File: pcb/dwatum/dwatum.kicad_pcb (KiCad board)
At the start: 2 copper layers, 0 parts

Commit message: starting on layout
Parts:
- added A1: ANT, polypoint:FRACTUS-2.4GHZ-FR05-S1-N-0-102, F.Cu at (193.1, 106.5)
- added B1: 2450BM15A0002, polypoint:2450BM, F.Cu at (172.4, 106.0)
- added C1: 1uF, Capacitors_SMD:C_0402, F.Cu at (196.8, 135.9)
- added C10: 22pF, Capacitors_SMD:C_0402, F.Cu at (195.9, 118.8)
- added C11: 22pF, Capacitors_SMD:C_0402, F.Cu at (189.2, 124.1)
- added C12: 12pF, Capacitors_SMD:C_0402, F.Cu at (200.6, 111.4)
- added C13: 12pF, Capacitors_SMD:C_0402, F.Cu at (183.6, 128.0)
- added C14: 1uF, Capacitors_SMD:C_0402, F.Cu at (204.6, 105.7)
- added C15: 1uF, Capacitors_SMD:C_0402, F.Cu at (192.0, 118.4)
- added C16: 1uF, Capacitors_SMD:C_0402, F.Cu at (196.8, 113.3)
- added C17: 1uF, Capacitors_SMD:C_0402, F.Cu at (179.8, 129.2)
- added C18: 10uF, Capacitors_SMD:C_0603, F.Cu at (185.7, 116.6)
- added C19: 10uF, Capacitors_SMD:C_0603, F.Cu at (176.0, 124.9)
- added C2: 0.1uF, Capacitors_SMD:C_0402, F.Cu at (205.6, 116.9)
- added C20: 1nF, Capacitors_SMD:C_0402, F.Cu at (208.0, 105.7)
- added C3: 0.1uF, Capacitors_SMD:C_0402, F.Cu at (198.4, 124.3)
- added C4: 0.1uF, Capacitors_SMD:C_0402, F.Cu at (193.7, 124.3)
- added C5: 0.1uF, Capacitors_SMD:C_0402, F.Cu at (189.0, 129.6)
- added C6: 0.1uF, Capacitors_SMD:C_0402, F.Cu at (200.9, 116.9)
- added C7: 220pF, Capacitors_SMD:C_0402, F.Cu at (184.1, 133.5)
- added C8: 0.1uF, Capacitors_SMD:C_0402, F.Cu at (205.1, 111.4)
- added C9: 0.1uF, Capacitors_SMD:C_0402, F.Cu at (196.8, 133.3)
- added D1: Led_RGB_CA, polypoint:1mm_SQ_4PAD, F.Cu at (169.1, 124.6)
- added J1: TC2030-CC2538-BL, polypoint:TC2030, F.Cu at (158.0, 106.5)
- added L1: 2.2uH, polypoint:MIPSZ201D, F.Cu at (203.2, 122.2)
- added P1: CONN_01X02, Pin_Headers:Pin_Header_Straight_1x02, F.Cu at (184.2, 109.1)
- added R1: 10K, Resistors_SMD:R_0402, F.Cu at (185.3, 122.4)
- added R2: 10K, Resistors_SMD:R_0402, F.Cu at (179.8, 123.6)
- added R3: 2.2K, Resistors_SMD:R_0402, F.Cu at (174.4, 130.7)
- added R4: 56K, Resistors_SMD:R_0402, F.Cu at (201.1, 105.8)
- added R5: 1K, Resistors_SMD:R_0402, F.Cu at (198.2, 105.8)
- added R6: 1K, Resistors_SMD:R_0402, F.Cu at (171.2, 130.2)
- added R7: 1K, Resistors_SMD:R_0402, F.Cu at (189.1, 118.5)
- added U1: DWM1000, polypoint:DWM1000_REVERSE, F.Cu at (157.1, 123.4)
- added U2: CC2538, polypoint:QFN-56-1EP_8x8mm_Pitch0.5mm, F.Cu at (157.5, 116.8)
- added U3: TPS727xx, polypoint:WSON-8_1.5x1.5mm, F.Cu at (166.1, 130.4)
- added U4: TPS62740, polypoint:R-PWSON-12, F.Cu at (179.6, 117.2)
- added X1: CRYSTAL_SMD_4, polypoint:FA-128, F.Cu at (156.0, 130.0)
- added Y1: Crystal, polypoint:ABS05, F.Cu at (192.2, 113.1)

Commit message: working on pcb placement
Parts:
- U1: footprint polypoint:DWM1000_REVERSE -> polypoint:DWM1000_REVERSE_SMD
- moved C1 65.4 mm to (171.8, 75.5), turned to 90 degrees
- moved C9 61.5 mm to (178.2, 74.8), turned to 270 degrees
- moved L1 58.1 mm to (162.8, 80.5), turned to 270 degrees
- moved C7 56.9 mm to (180.5, 76.8), turned to 270 degrees
- moved X1 54.8 mm to (184.2, 83.0), turned to 90 degrees
- moved C17 54.5 mm to (170.5, 75.5), turned to 90 degrees
- moved C5 53.4 mm to (181.5, 76.8), turned to 270 degrees
- moved C11 50.7 mm to (174.0, 75.8), turned to 180 degrees
- moved C10 49.4 mm to (174.0, 74.5)
- moved C6 47.6 mm to (167.8, 82.8), turned to 180 degrees
- moved C18 47.0 mm to (163.5, 75.2)
- moved C3 46.4 mm to (181.0, 81.2), turned to 180 degrees
- moved U3 46.2 mm to (164.0, 84.2), turned to 90 degrees
- moved C19 45.9 mm to (164.5, 80.5), turned to 90 degrees
- moved C15 45.3 mm to (162.2, 84.2), turned to 270 degrees
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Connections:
- C1 pad 1: +3V3 -> VCC
- C2 pad 1: +3V3 -> VCC
- C3 pad 2: +3V3 -> VCC
- C4 pad 1: +3V3 -> VCC
- C5 pad 2: +3V3 -> VCC
- C6 pad 1: +3V3 -> VCC
- C7 pad 2: +3V3 -> VCC
- C8 pad 1: +3V3 -> VCC
- C9 pad 2: +3V3 -> VCC
- U2 pad 10: +3V3 -> VCC
- U2 pad 15: +3V3 -> VCC
- U2 pad 24: +3V3 -> VCC
- U2 pad 30: LED_BLUE -> LED_GREEN
- U2 pad 31: LED_GREEN -> LED_BLUE
- U2 pad 33: +3V3 -> VCC
- U2 pad 36: +3V3 -> VCC
- U2 pad 40: +3V3 -> VCC
- U2 pad 43: +3V3 -> VCC
- U2 pad 55: +3V3 -> VCC
- X1 pad 2: Net-(C13-Pad1) -> GND
- X1 pad 3: GND -> Net-(C13-Pad1)
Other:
- board outline added: 37.5 x 17.5 mm
- copper layers 2 -> 4

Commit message: most of the routing is done with dwatum
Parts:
- moved P1 29.8 mm to (188.5, 86.0), turned to 0 degrees
- moved J1 6.59 mm to (164.9, 87.7), turned to 0 degrees
- moved A1 4.59 mm to (189.2, 76.2), turned to 90 degrees
- moved C2 0.75 mm to (175.2, 88.2)
- moved C20 0.75 mm to (176.8, 88.2)
- moved R3 0.75 mm to (178.2, 88.2)
- moved C4 0.68 mm to (170.1, 87.7), turned to 180 degrees
- moved C13 0.65 mm to (185.8, 83.0)
- moved D1 0.56 mm to (184.2, 86.8)
- moved U1 0.50 mm to (174.0, 85.5)
- moved X1 0.45 mm to (183.8, 83.0)
- moved C14 0.32 mm to (163.8, 86.0), turned to 0 degrees
- moved C1 0.25 mm to (171.8, 75.2)
- moved C17 0.25 mm to (170.5, 75.2)
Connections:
- U1 pad 5: VCC -> VAA
- U1 pad 6: VCC -> VAA
- U1 pad 7: VCC -> VAA
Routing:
- net +BATT: track 0.00 -> 56.3 mm
- net VAA: track 0.00 -> 47.3 mm, vias 0 -> 1
- net GND: track 0.00 -> 40.1 mm, vias 0 -> 39
- net DW_WAKEUP: track 0.00 -> 34.6 mm, vias 0 -> 3
- net VCC: track 0.00 -> 33.5 mm, vias 0 -> 10
- net ~RESET: track 0.00 -> 15.1 mm, vias 0 -> 3
- net BOOTLOADER_RX: track 0.00 -> 12.6 mm
- net BOOTLOADER_TX: track 0.00 -> 11.4 mm, vias 0 -> 2
- net BOOTLOADER_CTRL: track 0.00 -> 10.6 mm
- net DW_RSTn: track 0.00 -> 8.96 mm, vias 0 -> 1
- net Net-(C13-Pad1): track 0.00 -> 8.28 mm
- net SPI_SCK: track 0.00 -> 8.23 mm, vias 0 -> 1
- net Net-(C12-Pad2): track 0.00 -> 7.96 mm
- net Net-(B1-Pad4): track 0.00 -> 6.89 mm
- net Net-(B1-Pad3): track 0.00 -> 6.85 mm
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- added copper zone on In1.Cu, net GND
- added copper zone on In2.Cu, net VCC
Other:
- board size 37.5 x 17.5 mm -> 31 x 18.5 mm
- rule trace_min: 0.2 -> 0.1524
- rule via_min_drill: 0.3 -> 0.2032
- rule via_min_size: 0.4 -> 0.508
- board text added: "Ben Kempke"
- board text added: "DW1000"
- board text added: "DWAtum v0.1"
- board text added: "Univ. of Mich."

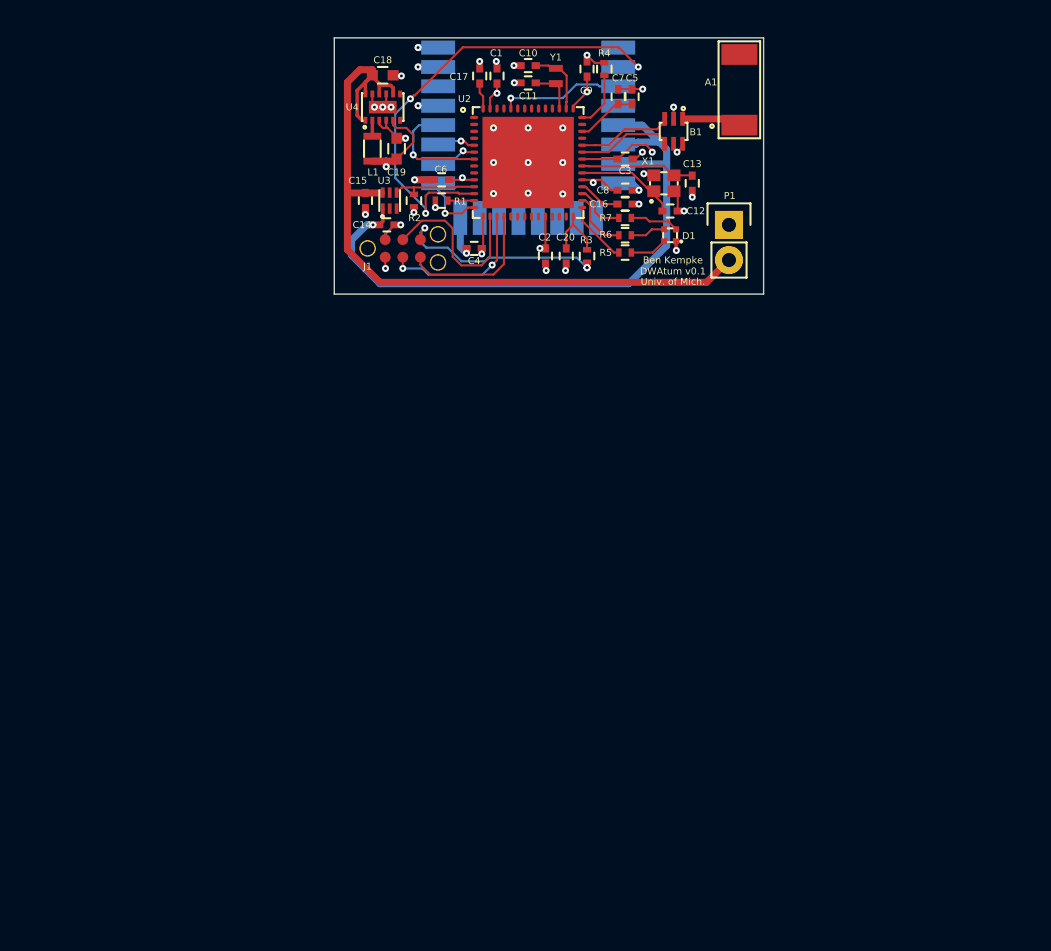
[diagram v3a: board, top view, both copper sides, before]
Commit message: adding atum footprint and starting from scratch with dwatum adapter board
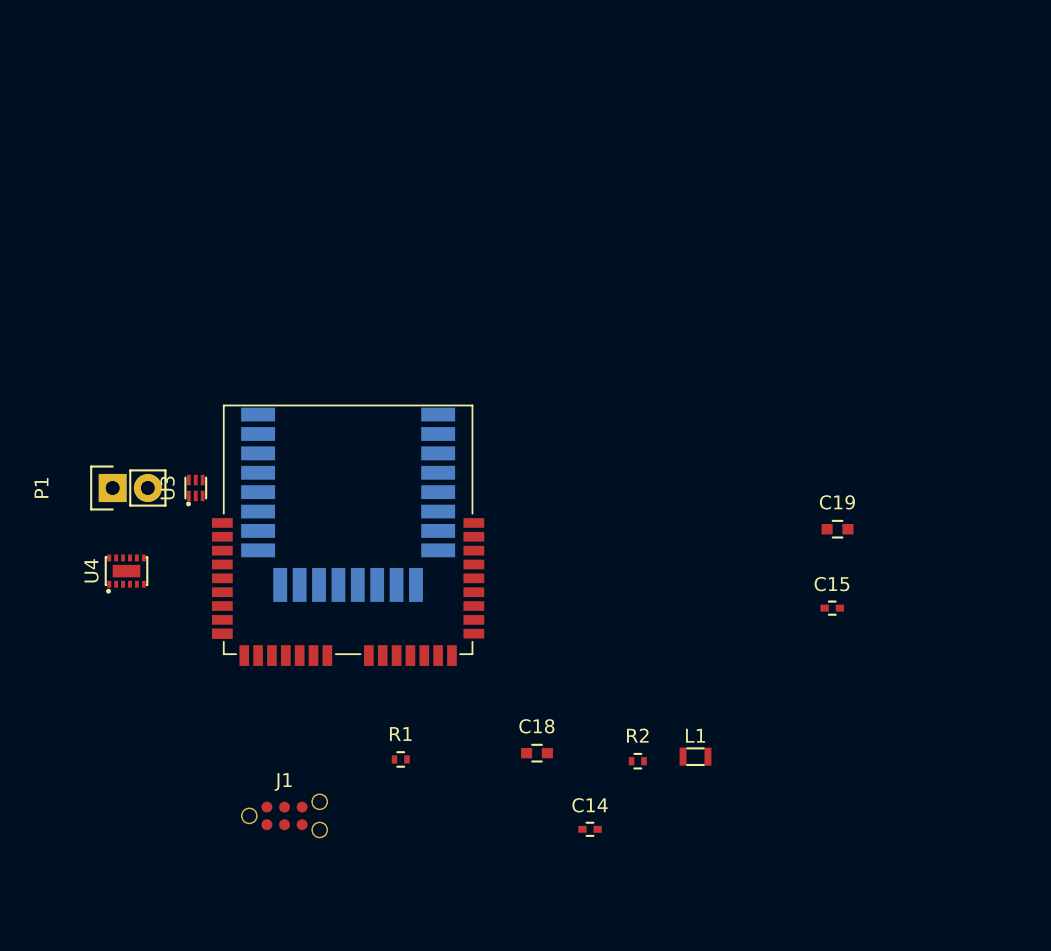
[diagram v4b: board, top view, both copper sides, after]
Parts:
- removed A1: ANT, polypoint:FRACTUS-2.4GHZ-FR05-S1-N-0-102
- removed B1: 2450BM15A0002, polypoint:2450BM
- removed C1, C16, C17: 1uF, Capacitors_SMD:C_0402
- removed C10, C11: 22pF, Capacitors_SMD:C_0402
- removed C12, C13: 12pF, Capacitors_SMD:C_0402
- removed C2, C3, C4, C5, C6, C8, C9: 0.1uF, Capacitors_SMD:C_0402
- removed C20: 1nF, Capacitors_SMD:C_0402
- removed C7: 220pF, Capacitors_SMD:C_0402
- removed D1: Led_RGB_CA, polypoint:1mm_SQ_4PAD
- removed R3: 2.2K, Resistors_SMD:R_0402
- removed R4: 56K, Resistors_SMD:R_0402
- removed R5, R6, R7: 1K, Resistors_SMD:R_0402
- removed X1: CRYSTAL_SMD_4, polypoint:FA-128
- removed Y1: Crystal, polypoint:ABS05
- U2: value CC2538 -> ATUM; footprint polypoint:QFN-56-1EP_8x8mm_Pitch0.5mm -> polypoint:ATUM_SMD
- moved C18 50.2 mm to (174.6, 124.1)
- moved L1 49.7 mm to (186.1, 124.4), turned to 0 degrees
- moved P1 48.4 mm to (144.0, 105.0), turned to 90 degrees
- moved C14 46.0 mm to (178.5, 129.6)
- moved C15 44.7 mm to (196.0, 113.7), turned to 0 degrees
- moved R2 43.6 mm to (181.9, 124.7), turned to 0 degrees
- moved C19 42.1 mm to (196.3, 108.0), turned to 0 degrees
- moved J1 41.9 mm to (156.4, 128.7)
- moved R1 40.5 mm to (164.8, 124.6), turned to 0 degrees
- moved U4 38.3 mm to (145.0, 111.0)
- moved U2 37.8 mm to (161.0, 117.0), turned to 270 degrees
- moved U1 29.5 mm to (161.0, 112.0)
- moved U3 25.0 mm to (150.0, 105.0)
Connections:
- U2 pad 1: Net-(U2-Pad1) -> VCC
- U2 pad 10: VCC -> Net-(U2-Pad10)
- U2 pad 11: DW_PWR_EN -> Net-(U2-Pad11)
- U2 pad 12: DW_WAKEUP -> Net-(U2-Pad12)
- U2 pad 13: DW_IRQ -> Net-(U2-Pad13)
- U2 pad 14: DW_CE -> SPI_MISO
- U2 pad 15: VCC -> SPI_MOSI
- U2 pad 16: BOOTLOADER_RX -> SPI_SCK
- U2 pad 17: BOOTLOADER_TX -> Net-(U2-Pad17)
- U2 pad 18: BOOTLOADER_CTRL -> Net-(U2-Pad18)
- U2 pad 19: Net-(U2-Pad19) -> DW_WAKEUP
- U2 pad 20: Net-(U2-Pad20) -> DW_IRQ
- U2 pad 21: Net-(U2-Pad21) -> DW_CE
- U2 pad 22: Net-(U2-Pad22) -> BOOTLOADER_RX
- U2 pad 23: Net-(U2-Pad23) -> BOOTLOADER_TX
- U2 pad 24: VCC -> BOOTLOADER_CTRL
- U2 pad 29: LED_RED -> Net-(U2-Pad29)
- U2 pad 30: LED_GREEN -> ~RESET
- U2 pad 31: LED_BLUE -> Net-(U2-Pad31)
- U2 pad 32: Net-(C16-Pad1) -> GND
- U2 pad 5: SPI_MISO -> Net-(U2-Pad5)
- U2 pad 6: SPI_MOSI -> Net-(U2-Pad6)
- U2 pad 7: SPI_SCK -> Net-(U2-Pad7)
- U2 pad 8: Net-(U2-Pad8) -> DW_PWR_EN
- U2 pad 9: Net-(U2-Pad9) -> DW_RSTn
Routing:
- net +BATT: track 56.3 -> 0.00 mm
- net VAA: track 47.3 -> 0.00 mm, vias 1 -> 0
- net GND: track 40.1 -> 0.00 mm, vias 39 -> 0
- net DW_WAKEUP: track 34.6 -> 0.00 mm, vias 3 -> 0
- net VCC: track 33.5 -> 0.00 mm, vias 10 -> 0
- net ~RESET: track 15.1 -> 0.00 mm, vias 3 -> 0
- net BOOTLOADER_RX: track 12.6 -> 0.00 mm
- net BOOTLOADER_TX: track 11.4 -> 0.00 mm, vias 2 -> 0
- net BOOTLOADER_CTRL: track 10.6 -> 0.00 mm
- net DW_RSTn: track 8.96 -> 0.00 mm, vias 1 -> 0
- net Net-(C13-Pad1): track 8.28 -> 0.00 mm
- net SPI_SCK: track 8.23 -> 0.00 mm, vias 1 -> 0
- net Net-(C12-Pad2): track 7.96 -> 0.00 mm
- net Net-(B1-Pad4): track 6.89 -> 0.00 mm
- net Net-(B1-Pad3): track 6.85 -> 0.00 mm
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- removed copper zone on In1.Cu, net GND
- removed copper zone on In2.Cu, net VCC
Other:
- board outline removed
- copper layers 4 -> 2
- rule pad_to_mask_clearance: 0 -> 0.2
- rule trace_min: 0.1524 -> 0.2
- rule via_min_drill: 0.2032 -> 0.3
- rule via_min_size: 0.508 -> 0.4
- board text removed: "Ben Kempke"
- board text removed: "DW1000"
- board text removed: "DWAtum v0.1"
- board text removed: "Univ. of Mich."

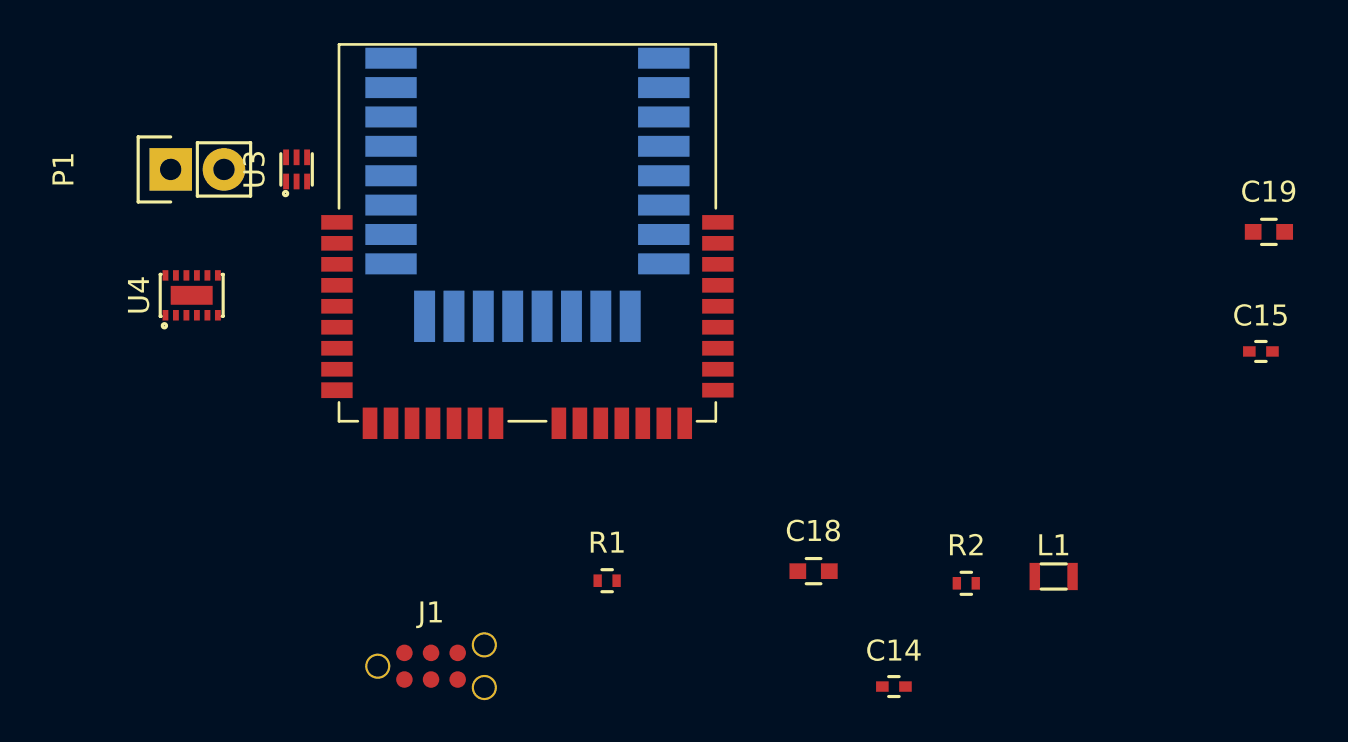
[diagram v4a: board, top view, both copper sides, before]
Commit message: better placement
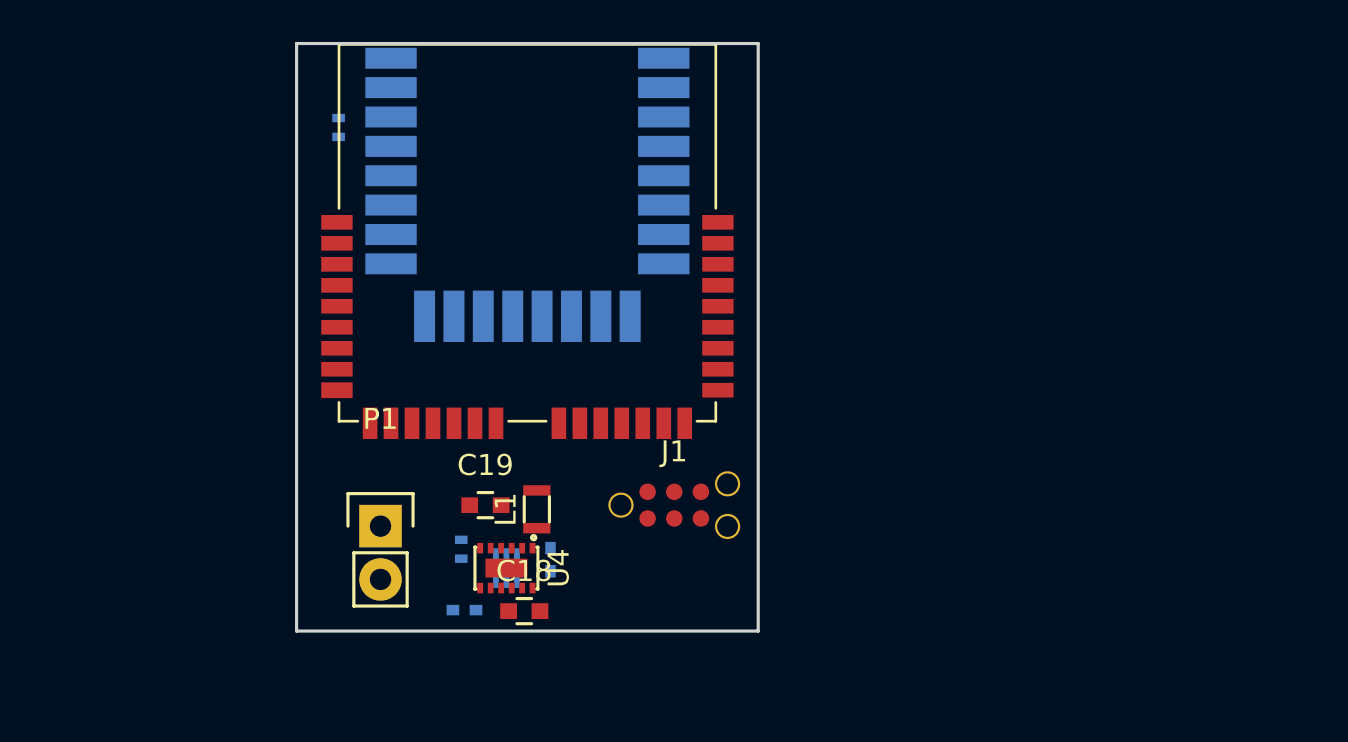
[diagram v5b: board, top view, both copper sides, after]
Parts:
- C14, C15, R1, R2, U3: moved to B.Cu
- moved C15 39.9 mm to (158.0, 126.0)
- moved C19 39.5 mm to (159.0, 121.0)
- moved R1 25.1 mm to (152.0, 103.0), turned to 270 degrees
- moved L1 24.8 mm to (161.4, 121.2), turned to 90 degrees
- moved R2 24.1 mm to (157.8, 123.1), turned to 270 degrees
- moved U3 21.5 mm to (160.0, 124.0)
- moved U4 19.8 mm to (160.0, 124.0), turned to 270 degrees
- moved P1 19.7 mm to (154.0, 122.0), turned to 0 degrees
- moved C14 17.4 mm to (162.1, 123.6), turned to 90 degrees
- moved C18 13.9 mm to (160.8, 126.0)
- moved J1 13.9 mm to (168.0, 121.0)
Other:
- board outline added: 22 x 28 mm
